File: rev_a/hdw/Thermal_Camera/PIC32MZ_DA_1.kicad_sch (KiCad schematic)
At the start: 3 parts

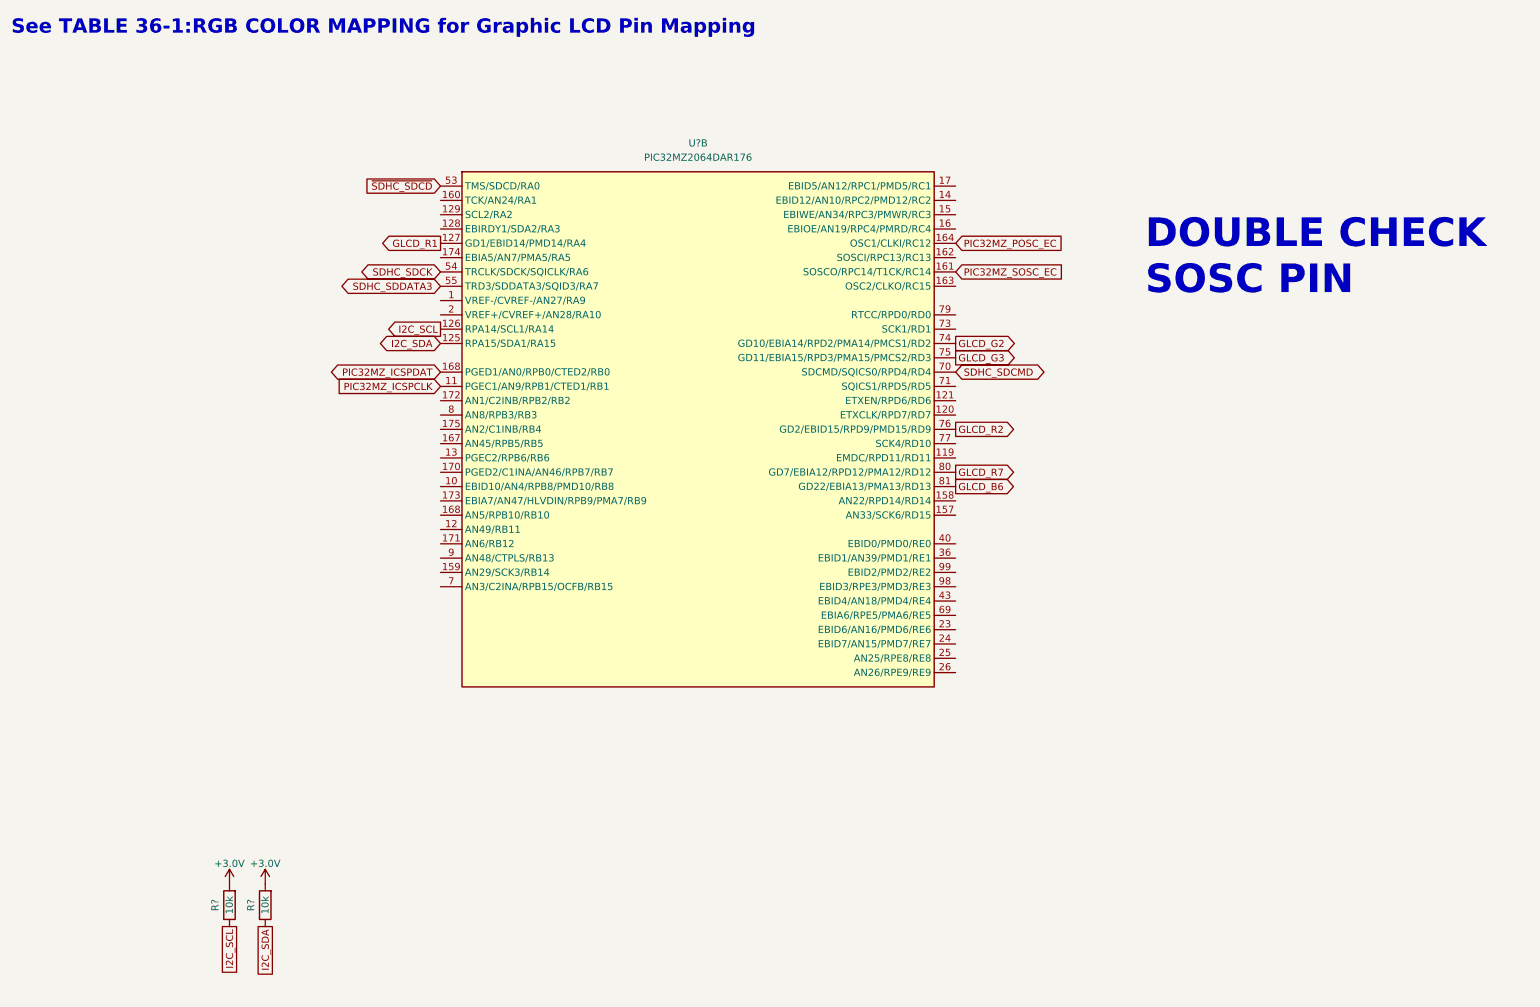
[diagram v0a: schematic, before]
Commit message: assigned some GPIO pins
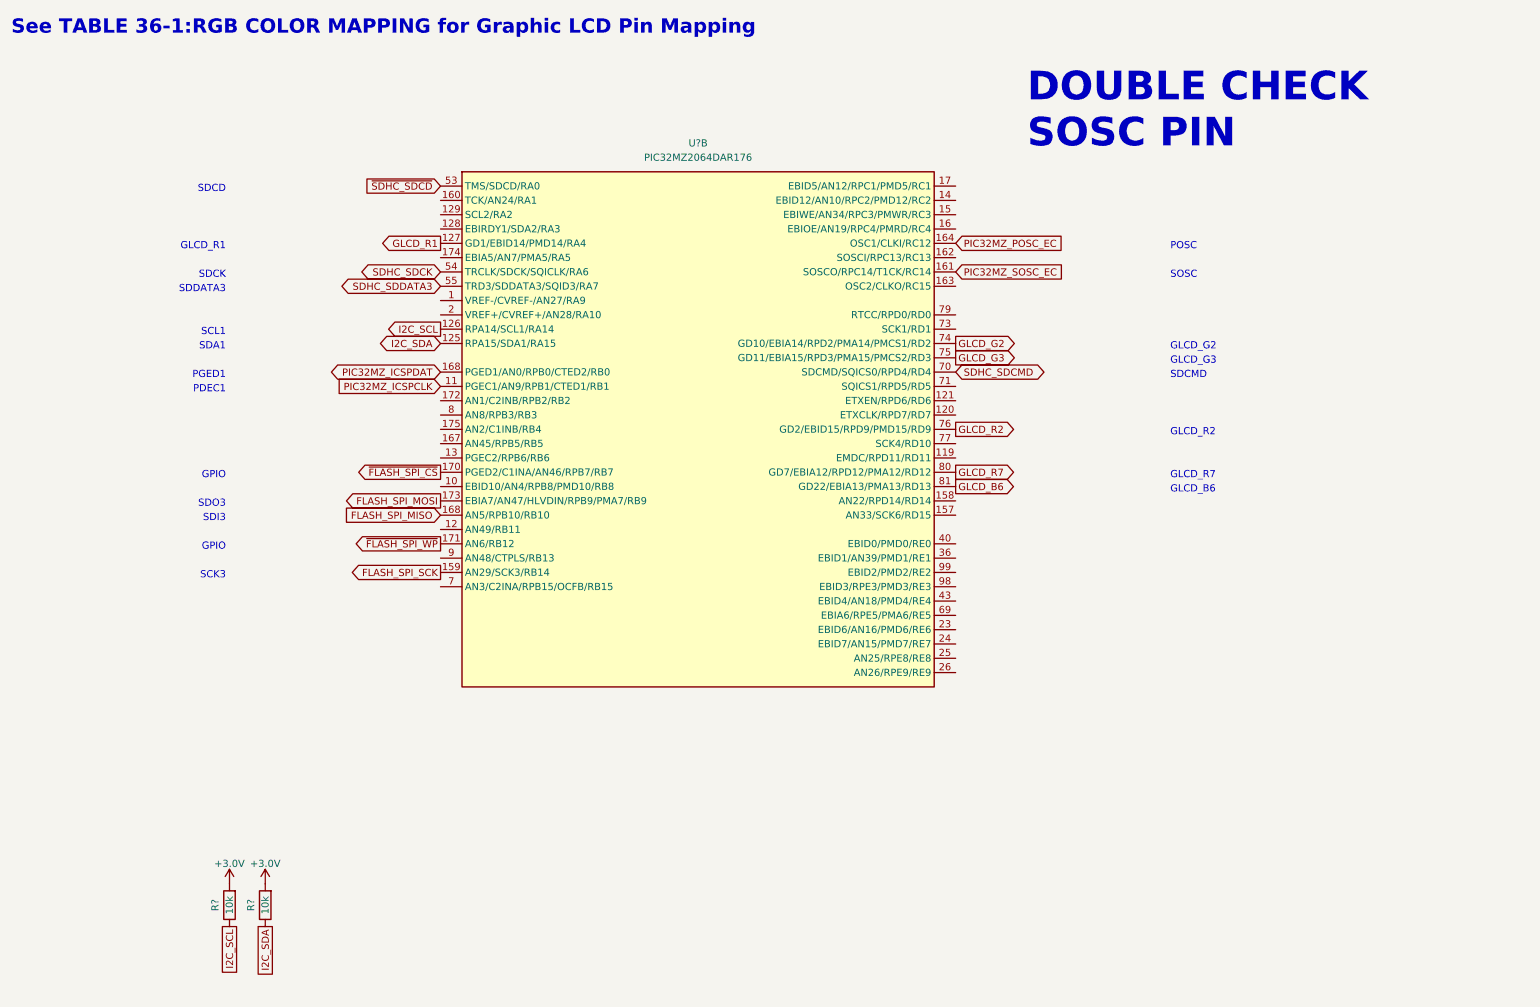
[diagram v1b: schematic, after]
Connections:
- net FLASH_SPI_SCK: now reaches U?.159 (AN29/SCK3/RB14)
- net ~{FLASH_SPI_CS}: now reaches U?.170 (PGED2/C1INA/AN46/RPB7/RB7)
- net ~{FLASH_SPI_WP}: now reaches U?.171 (AN6/RB12)
- net FLASH_SPI_MOSI: now reaches U?.173 (EBIA7/AN47/HLVDIN/RPB9/PMA7/RB9)
- new net FLASH_SPI_MISO: U?.168 (PGED1/AN0/RPB0/CTED2/RB0)
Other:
- note added: "GLCD_B6"
- note added: "GLCD_G2"
- note added: "GLCD_G3"
- note added: "GLCD_R1"
- note added: "GLCD_R2"
- note added: "GLCD_R7"
- note added: "GPIO"
- note added: "PDEC1"
- note added: "PGED1"
- note added: "POSC"
- note added: "SCK3"
- note added: "SCL1"
- note added: "SDA1"
- note added: "SDCD"
- note added: "SDCK"
- note added: "SDCMD"
- note added: "SDDATA3"
- note added: "SDI3"
- note added: "SDO3"
- note added: "SOSC"
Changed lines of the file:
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@@
     (company "Drew Maatman and Michael Laffin")
   )
-  (text "DOUBLE CHECK\nSOSC PIN" (at 216.535 64.135 0)
+  (text "PGED1" (at 53.34 78.74 0)
+    (effects (font (size 1.27 1.27)) (justify right bottom))
+  )
+  (text "POSC" (at 220.98 55.88 0)
+    (effects (font (size 1.27 1.27)) (justify left bottom))
+  )
+  (text "GPIO" (at 53.34 109.22 0)
+    (effects (font (size 1.27 1.27)) (justify right bottom))
+  )
+  (text "SDCMD" (at 220.98 78.74 0)
+    (effects (font (size 1.27 1.27)) (justify left bottom))
+  )
+  (text "SOSC" (at 220.98 60.96 0)
+    (effects (font (size 1.27 1.27)) (justify left bottom))
+  )
+  (text "SDO3" (at 53.34 101.6 0)
+    (effects (font (size 1.27 1.27)) (justify right bottom))
+  )
+  (text "DOUBLE CHECK\nSOSC PIN" (at 195.58 38.1 0)
     (effects (font (size 5.08 5.08) (thickness 1.016) bold (color 194 0 0 1)) (justify left bottom))
+  )
+  (text "SDCK" (at 53.34 60.96 0)
+    (effects (font (size 1.27 1.27)) (justify right bottom))
+  )
+  (text "SCL1" (at 53.34 71.12 0)
+    (effects (font (size 1.27 1.27)) (justify right bottom))
+  )
+  (text "GLCD_G3" (at 220.98 76.2 0)
+    (effects (font (size 1.27 1.27)) (justify left bottom))
+  )
+  (text "GPIO" (at 53.34 96.52 0)
+    (effects (font (size 1.27 1.27)) (justify right bottom))
+  )
+  (text "GLCD_B6" (at 220.98 99.06 0)
+    (effects (font (size 1.27 1.27)) (justify left bottom))
+  )
+  (text "SDI3" (at 53.34 104.14 0)
+    (effects (font (size 1.27 1.27)) (justify right bottom))
+  )
+  (text "SDDATA3" (at 53.34 63.5 0)
+    (effects (font (size 1.27 1.27)) (justify right bottom))
+  )
+  (text "GLCD_R2" (at 220.98 88.9 0)
+    (effects (font (size 1.27 1.27)) (justify left bottom))
+  )
+  (text "GLCD_G2" (at 220.98 73.66 0)
+    (effects (font (size 1.27 1.27)) (justify left bottom))
+  )
+  (text "PDEC1" (at 53.34 81.28 0)
+    (effects (font (size 1.27 1.27)) (justify right bottom))
+  )
+  (text "SDCD" (at 53.34 45.72 0)
+    (effects (font (size 1.27 1.27)) (justify right bottom))
+  )
+  (text "GLCD_R7" (at 220.98 96.52 0)
+    (effects (font (size 1.27 1.27)) (justify left bottom))
+  )
+  (text "GLCD_R1" (at 53.34 55.88 0)
+    (effects (font (size 1.27 1.27)) (justify right bottom))
+  )
+  (text "SCK3" (at 53.34 114.3 0)
+    (effects (font (size 1.27 1.27)) (justify right bottom))
+  )
+  (text "SDA1" (at 53.34 73.66 0)
+    (effects (font (size 1.27 1.27)) (justify right bottom))
   )
   (text "See TABLE 36-1:RGB COLOR MAPPING for Graphic LCD Pin Mapping"
@@
     (property "Intersheetrefs" "${INTERSHEET_REFS}" (at 194.1504 97.79 0)
       (effects (font (size 1.27 1.27)) (justify left) hide)
+    )
+  )
+  (global_label "~{FLASH_SPI_CS}" (shape output) (at 91.44 95.25 180) (fields_autoplaced)
+    (effects (font (size 1.27 1.27)) (justify right))
+    (property "Intersheetrefs" "${INTERSHEET_REFS}" (at 75.2899 95.25 0)
+      (effects (font (size 1.27 1.27)) (justify right) hide)
     )
   )
@@
     )
   )
+  (global_label "FLASH_SPI_MOSI" (shape output) (at 91.44 100.33 180) (fields_autoplaced)
+    (effects (font (size 1.27 1.27)) (justify right))
+    (property "Intersheetrefs" "${INTERSHEET_REFS}" (at 73.1732 100.33 0)
+      (effects (font (size 1.27 1.27)) (justify right) hide)
+    )
+  )
   (global_label "I2C_SDA" (shape passive) (at 60.325 175.895 270) (fields_autoplaced)
     (effects (font (size 1.27 1.27)) (justify right))
@@
     (property "Intersheetrefs" "${INTERSHEET_REFS}" (at 199.495 77.47 0)
       (effects (font (size 1.27 1.27)) (justify left) hide)
+    )
+  )
+  (global_label "FLASH_SPI_SCK" (shape output) (at 91.44 113.03 180) (fields_autoplaced)
+    (effects (font (size 1.27 1.27)) (justify right))
+    (property "Intersheetrefs" "${INTERSHEET_REFS}" (at 74.0199 113.03 0)
+      (effects (font (size 1.27 1.27)) (justify right) hide)
+    )
+  )
+  (global_label "~{FLASH_SPI_WP}" (shape output) (at 91.44 107.95 180) (fields_autoplaced)
+    (effects (font (size 1.27 1.27)) (justify right))
+    (property "Intersheetrefs" "${INTERSHEET_REFS}" (at 75.048 107.95 0)
+      (effects (font (size 1.27 1.27)) (justify right) hide)
     )
   )
@@
       (effects (font (size 1.27 1.27)) (justify right) hide)
     )
+  )
+  (global_label "FLASH_SPI_MISO" (shape input) (at 91.44 102.87 180) (fields_autoplaced)
+    (effects (font (size 1.27 1.27)) (justify right))
+    (property "Intersheetrefs" "${INTERSHEET_REFS}" (at 73.1732 102.87 0)
+      (effects (font (size 1.27 1.27)) (justify right) hide)
+    )

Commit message: blah blah
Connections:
- net ~{FLASH_SPI_CS}: now also U?.175 (AN2/C1INB/RB4); no longer U?.170 (PGED2/C1INA/AN46/RPB7/RB7)
- net PIC32MZ_REFCLK1: now reaches U?.119 (EMDC/RPD11/RD11)
- net FLIR_VOSPI_MISO: now reaches U?.120 (ETXCLK/RPD7/RD7)
- net ~{FLIR_PWR_DWN}: now reaches U?.121 (ETXEN/RPD6/RD6)
- net USB_UART_RX: now reaches U?.13 (PGEC2/RPB6/RB6)
- net Reset_LED: now reaches U?.14 (EBID12/AN10/RPC2/PMD12/RC2)
- net CPU_Trap_LED: now reaches U?.15 (EBIWE/AN34/RPC3/PMWR/RC3)
- net ~{FLIR_RESET}: now reaches U?.157 (AN33/SCK6/RD15)
- net FLIR_CLK_EN: now reaches U?.158 (AN22/RPD14/RD14)
- net Heartbeat_LED: now reaches U?.16 (EBIOE/AN19/RPC4/PMRD/RC4)
- net BACKLIGHT_PWM: now reaches U?.167 (AN45/RPB5/RB5)
- net Error_LED: now reaches U?.17 (EBID5/AN12/RPC1/PMD5/RC1)
- net ~{USB_UART_RTS}: now reaches U?.172 (AN1/C2INB/RPB2/RB2)
- net ~{BATT_CEN}: now reaches U?.23 (EBID6/AN16/PMD6/RE6)
- net BATT_IUSB: now reaches U?.24 (EBID7/AN15/PMD7/RE7)
- net BATT_LOWBAT: now reaches U?.25 (AN25/RPE8/RE8)
- net ~{BATT_UOK}: now reaches U?.36 (EBID1/AN39/PMD1/RE1)
- net ~{BATT_FLT}: now reaches U?.40 (EBID0/PMD0/RE0)
- net FLIR_VOSPI_MOSI: now reaches U?.71 (SQICS1/RPD5/RD5)
- net ~{FLIR_VOSPI_CS}: now reaches U?.73 (SCK1/RD1)
- net FLIR_VOSPI_CLK: now reaches U?.77 (SCK4/RD10)
- net FLIR_VOSPI_VSYNC: now reaches U?.79 (RTCC/RPD0/RD0)
- net USB_UART_TX: now reaches U?.8 (AN8/RPB3/RB3)
- net ~{BATT_CHG}: now reaches U?.98 (EBID3/RPE3/PMD3/RE3)
- net ~{BATT_DOK}: now reaches U?.99 (EBID2/PMD2/RE2)
- new net ~{USB_UART_CTS}: U?.170 (PGED2/C1INA/AN46/RPB7/RB7)
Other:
- note added: "INT1"
- note added: "OC3"
- note added: "OC5"
- note added: "REFCLKO1"
- note added: "SCK4"
- note added: "SDI4"
- note added: "SDO4"
- note added: "U5CTS"
- note added: "U5RTS"
- note added: "U5RX"
- note added: "U5TX"

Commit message: some stuff
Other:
- note removed: "DOUBLE CHECK SOSC PIN"
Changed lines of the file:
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@@
-		)
-	)
-	(text "DOUBLE CHECK\nSOSC PIN"
-		(exclude_from_sim no)
-		(at 170.434 32.258 0)
-		(effects
-			(font
-				(size 5.08 5.08)
-				(thickness 1.016)
-				(bold yes)
-				(color 194 0 0 1)
-			)
-			(justify left bottom)
 		)
 	)

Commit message: lots of schematic progress
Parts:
- R? (x2): footprint Resistors_SMD:R_0603 -> (none); Digi-Key PN 541-10.0KHCT-ND -> (none); Wattage 1/10W -> (none); display_footprint 0603 -> (none)
- gave numbers to parts that had none: 1
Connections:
- net PIC32MZ_ICSPDAT: now also U1801.169 (PGED1/AN0/RPB0/CTED2/RB0); no longer U1801.168 (PGED1/AN0/RPB0/CTED2/RB0)
- net Cap_Touch_Power: now reaches U1801.1 (VREF-/CVREF-/AN27/RA9)
- net Cap_Touch_Shutter: now reaches U1801.2 (VREF+/CVREF+/AN28/RA10)
- no-connect marks 0 -> 13
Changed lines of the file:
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@@
 	(title_block
 		(title "Thermal Camera")
-		(date "2023-12-07")
+		(date "2024-05-24")
 		(rev "PRELIM")
 		(company "Drew Maatman and Michael Laffin")
 	)
+	(no_connect
+		(at 91.44 115.57)
+	)
+	(no_connect
+		(at 91.44 57.15)
+	)
+	(no_connect
+		(at 182.88 130.81)
+	)
+	(no_connect
+		(at 182.88 57.15)
+	)
+	(no_connect
+		(at 91.44 105.41)
+	)
+	(no_connect
+		(at 91.44 52.07)
+	)
+	(no_connect
+		(at 182.88 120.65)
+	)
+	(no_connect
+		(at 91.44 46.99)
+	)
+	(no_connect
+		(at 91.44 110.49)
+	)
+	(no_connect
+		(at 91.44 97.79)
+	)
+	(no_connect
+		(at 91.44 49.53)
+	)
+	(no_connect
+		(at 182.88 62.23)
+	)
+	(no_connect
+		(at 182.88 118.11)
+	)
 	(text "PGED1"
 		(exclude_from_sim no)
@@
 		)
 	)
+	(text "GPIO"
+		(exclude_from_sim no)
+		(at 53.34 68.58 0)
+		(effects
+			(font
+				(size 1.27 1.27)
+			)
+			(justify right bottom)
+		)
+	)
 	(text "OC5"
 		(exclude_from_sim no)
@@
 		(exclude_from_sim no)
 		(at 53.34 93.98 0)
+		(effects
+			(font
+				(size 1.27 1.27)
+			)
+			(justify right bottom)
+		)
+	)
+	(text "GPIO"
+		(exclude_from_sim no)
+		(at 53.34 66.04 0)
 		(effects
 			(font
@@
 		)
 	)
+	(global_label "Cap_Touch_Shutter"
+		(shape input)
+		(at 91.44 67.31 180)
+		(effects
+			(font
+				(size 1.27 1.27)
+			)
+			(justify right)
+		)
+		(property "Intersheetrefs" "${INTERSHEET_REFS}"
+			(at 91.44 67.31 0)
+			(effects
+				(font
+					(size 1.27 1.27)
+				)
+				(hide yes)
+			)
+		)
+	)
 	(global_label "FLIR_VOSPI_CLK"
 		(shape output)
@@
 				)
 				(justify left)
+				(hide yes)
+			)
+		)
+	)
+	(global_label "Cap_Touch_Power"
+		(shape input)
+		(at 91.44 64.77 180)
+		(effects
+			(font
+				(size 1.27 1.27)
+			)
+			(justify right)
+		)
+		(property "Intersheetrefs" "${INTERSHEET_REFS}"
+			(at 91.44 64.77 0)
+			(effects
+				(font
+					(size 1.27 1.27)
+				)
 				(hide yes)
 			)
@@
 		(on_board yes)
 		(dnp no)
-		(property "Reference" "U?"
+		(property "Reference" "U1801"
 			(at 137.16 36.83 0)
 			(effects
@@
 		(pin "168"
 		)
-		(pin "168"
+		(pin "169"
 		)
 		(pin "17"
@@
 			(project "Thermal_Camera"
 				(path "/4bd21e0b-5408-4b93-866e-c82ac5b31fa9/1b710e3d-a955-405b-a057-cf08e93463c9"
-					(reference "U?")
+					(reference "U1801")
 					(unit 2)
 				)
@@
 		(on_board yes)
 		(dnp no)
-		(property "Reference" "#PWR01810"
+		(property "Reference" "#PWR01813"
 			(at 60.325 172.085 0)
 			(effects
@@
 			(project "Thermal_Camera"
 				(path "/4bd21e0b-5408-4b93-866e-c82ac5b31fa9/1b710e3d-a955-405b-a057-cf08e93463c9"
-					(reference "#PWR01810")
+					(reference "#PWR01813")
 					(unit 1)
 				)
@@
 			)
 		)
-		(property "Footprint" "Resistors_SMD:R_0603"
+		(property "Footprint" ""
 			(at 53.975 172.085 0)
 			(effects
@@
 			)
 		)
-		(property "display_footprint" "0603"
+		(property "display_footprint" ""
 			(at 56.515 169.799 0)
 			(effects
@@
 			)
 		)
-		(property "Wattage" "1/10W"
+		(property "Wattage" ""
 			(at 56.769 174.117 0)
 			(effects
@@
 			)
 		)
-		(property "Digi-Key PN" "541-10.0KHCT-ND"
+		(property "Digi-Key PN" ""
 			(at 61.595 161.925 0)
 			(effects
@@
 			(project "Nixie_Clock_Core"
 				(path "/16fdce21-b570-4d81-a458-e8839d611806/4cb440c2-4356-400c-9387-edaaa635d5a5"
-					(reference "R1305")
+					(reference "R?")
 					(unit 1)
 				)
@@
 			(project "Thermal_Camera"
 				(path "/4bd21e0b-5408-4b93-866e-c82ac5b31fa9/1b710e3d-a955-405b-a057-cf08e93463c9"
-					(reference "R?")
+					(reference "R1801")
 					(unit 1)
 				)
@@
 		(on_board yes)
 		(dnp no)
-		(property "Reference" "#PWR01809"
+		(property "Reference" "#PWR01812"
 			(at 53.975 172.085 0)
 			(effects
@@
 			(project "Thermal_Camera"
 				(path "/4bd21e0b-5408-4b93-866e-c82ac5b31fa9/1b710e3d-a955-405b-a057-cf08e93463c9"
-					(reference "#PWR01809")
+					(reference "#PWR01812")
 					(unit 1)
 				)
@@
 			)
 		)
-		(property "Footprint" "Resistors_SMD:R_0603"
+		(property "Footprint" ""
 			(at 60.325 172.085 0)
 			(effects
@@
 			)
 		)
-		(property "display_footprint" "0603"
+		(property "display_footprint" ""
 			(at 62.865 169.799 0)
 			(effects
@@
 			)
 		)
-		(property "Wattage" "1/10W"
+		(property "Wattage" ""
 			(at 63.119 174.117 0)
 			(effects
@@
 			)
 		)
-		(property "Digi-Key PN" "541-10.0KHCT-ND"
+		(property "Digi-Key PN" ""
 			(at 67.945 161.925 0)
 			(effects
@@
 			(project "Nixie_Clock_Core"
 				(path "/16fdce21-b570-4d81-a458-e8839d611806/4cb440c2-4356-400c-9387-edaaa635d5a5"
-					(reference "R1305")
+					(reference "R?")
 					(unit 1)
 				)
@@
 			(project "Thermal_Camera"
 				(path "/4bd21e0b-5408-4b93-866e-c82ac5b31fa9/1b710e3d-a955-405b-a057-cf08e93463c9"
-					(reference "R?")
+					(reference "R1802")
 					(unit 1)
 				)

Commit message: assigned a ton of footprints
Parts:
- R? (x2): footprint (none) -> Resistors_SMD:R_0402; Wattage (none) -> 1/16W; display_footprint (none) -> 0402
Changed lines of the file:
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@@
 			)
 		)
-		(property "Footprint" ""
+		(property "Footprint" "Resistors_SMD:R_0402"
 			(at 53.975 172.085 0)
 			(effects
@@
 			)
 		)
-		(property "display_footprint" ""
+		(property "display_footprint" "0402"
 			(at 56.515 169.799 0)
 			(effects
@@
 			)
 		)
-		(property "Wattage" ""
+		(property "Wattage" "1/16W"
 			(at 56.769 174.117 0)
 			(effects
@@
 			)
 		)
-		(property "Footprint" ""
+		(property "Footprint" "Resistors_SMD:R_0402"
 			(at 60.325 172.085 0)
 			(effects
@@
 			)
 		)
-		(property "display_footprint" ""
+		(property "display_footprint" "0402"
 			(at 62.865 169.799 0)
 			(effects
@@
 			)
 		)
-		(property "Wattage" ""
+		(property "Wattage" "1/16W"
 			(at 63.119 174.117 0)
 			(effects

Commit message: assigned resistor part numbers
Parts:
- R? (x2): Digi-Key PN (none) -> RMCF0402FT10K0CT-ND
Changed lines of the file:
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@@
 			)
 		)
-		(property "Digi-Key PN" ""
+		(property "Digi-Key PN" "RMCF0402FT10K0CT-ND"
 			(at 61.595 161.925 0)
 			(effects
@@
 			)
 		)
-		(property "Digi-Key PN" ""
+		(property "Digi-Key PN" "RMCF0402FT10K0CT-ND"
 			(at 67.945 161.925 0)
 			(effects

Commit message: hid passive refdes
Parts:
- renumbered U1801 to U1701
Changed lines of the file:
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@@
 		(on_board yes)
 		(dnp no)
-		(property "Reference" "U1801"
+		(property "Reference" "U1701"
 			(at 137.16 36.83 0)
 			(effects
@@
 			(project "Thermal_Camera"
 				(path "/4bd21e0b-5408-4b93-866e-c82ac5b31fa9/1b710e3d-a955-405b-a057-cf08e93463c9"
-					(reference "U1801")
+					(reference "U1701")
 					(unit 2)
 				)
